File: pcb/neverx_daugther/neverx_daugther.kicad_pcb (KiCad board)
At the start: 2 copper layers, 36.7 x 22 mm, 19 parts, among them J1 IN, J2 UL, J3 UR, J4 LL, J5 LR, Q1 BC807, U1 HX711

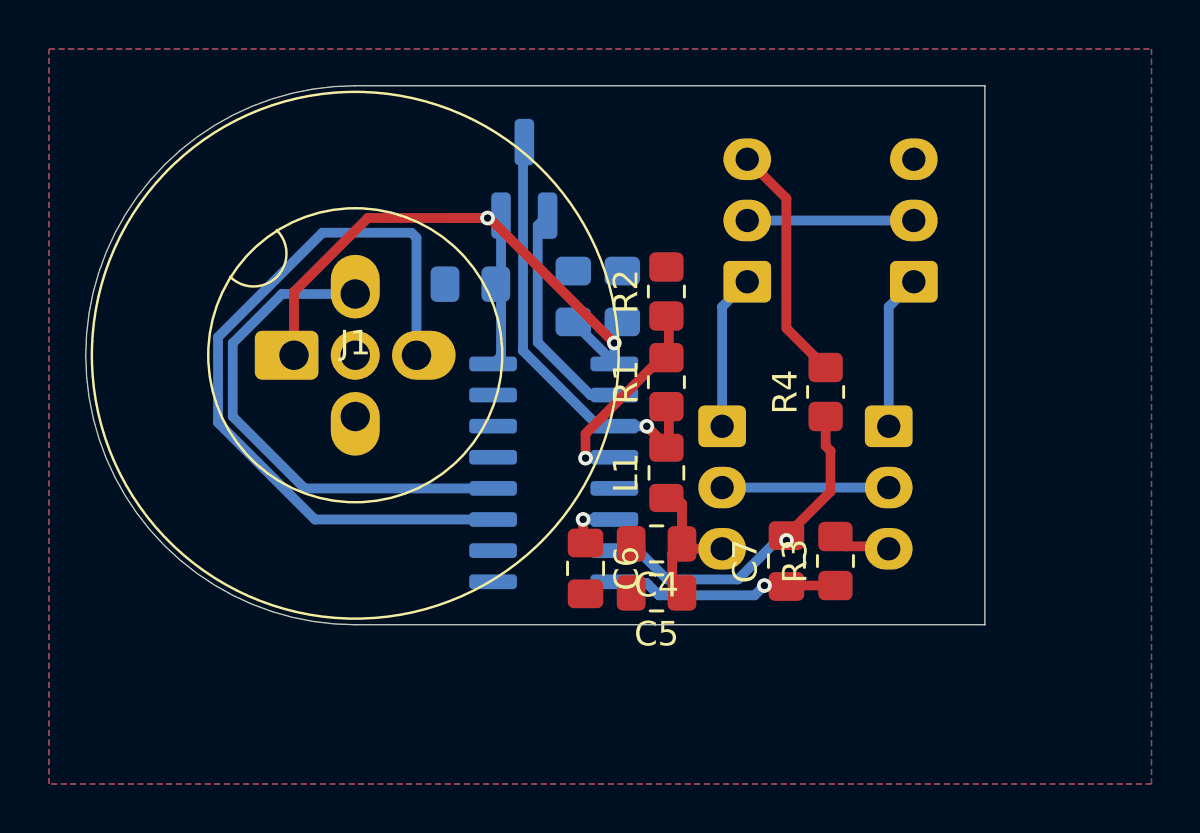
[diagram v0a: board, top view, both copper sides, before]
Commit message: Fixed wrongtraces
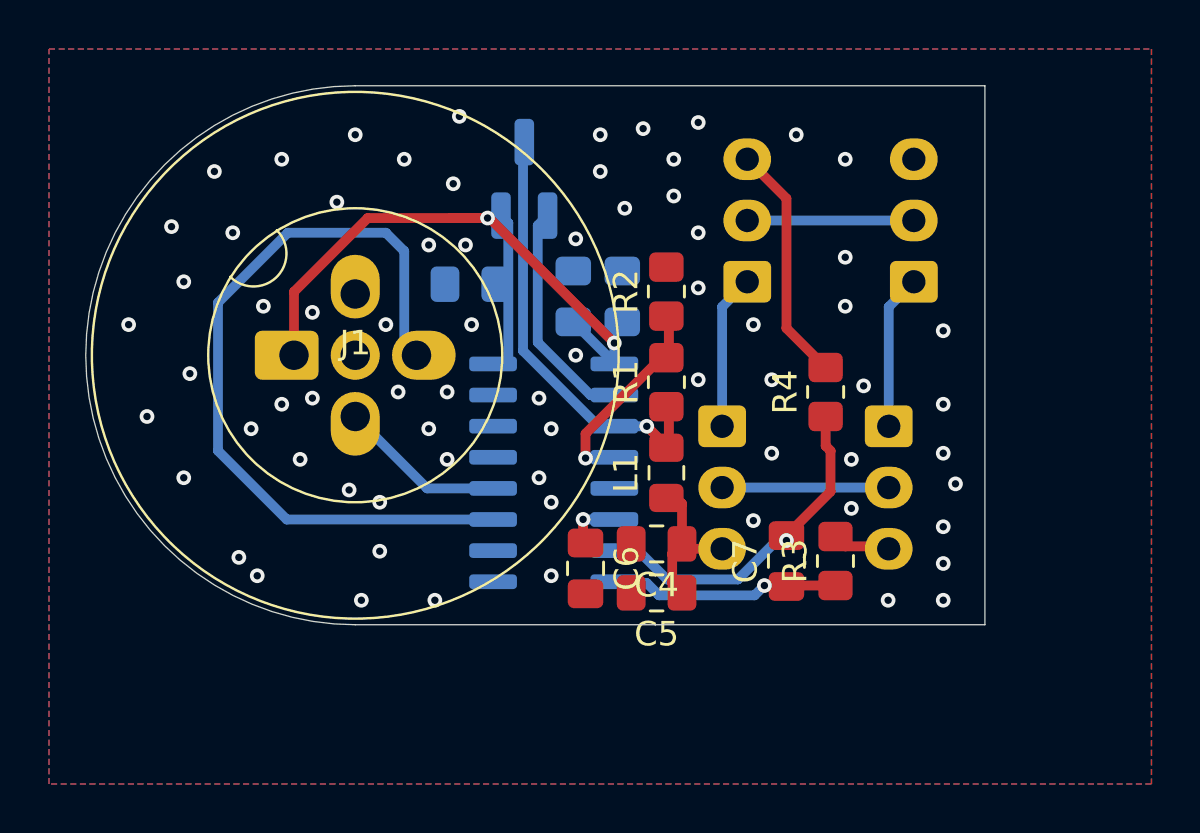
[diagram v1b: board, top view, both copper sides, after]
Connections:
- J1 pad 2: Net-(J1-Pin_2) -> E-
- J1 pad 4: unconnected-(J1-Pin_4-Pad4) -> Net-(J1-Pin_4)
- U1 pad 12: Net-(J1-Pin_2) -> Net-(J1-Pin_4)
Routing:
- net Net-(J1-Pin_2): track 20.7 -> 0.00 mm
- net Net-(J1-Pin_4): track 0.00 -> 6.84 mm
- net Net-(J1-Pin_3): track 31.1 -> 32.0 mm
- net +5V: track 31.6 -> 32.2 mm
- net E-: vias 0 -> 71
